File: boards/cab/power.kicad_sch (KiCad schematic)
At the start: 15 parts, among them U1 XL1509-5.0, U2 XL1509-ADJ

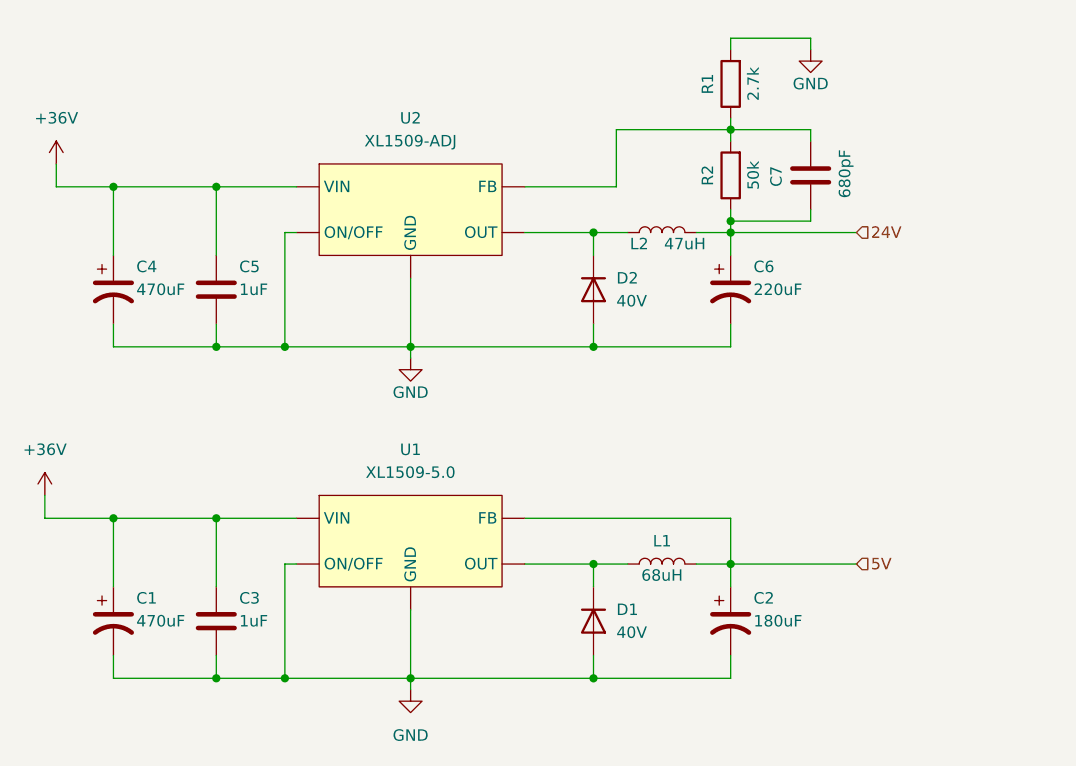
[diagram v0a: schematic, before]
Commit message: Removed hierarchy and added Connectors, Leds
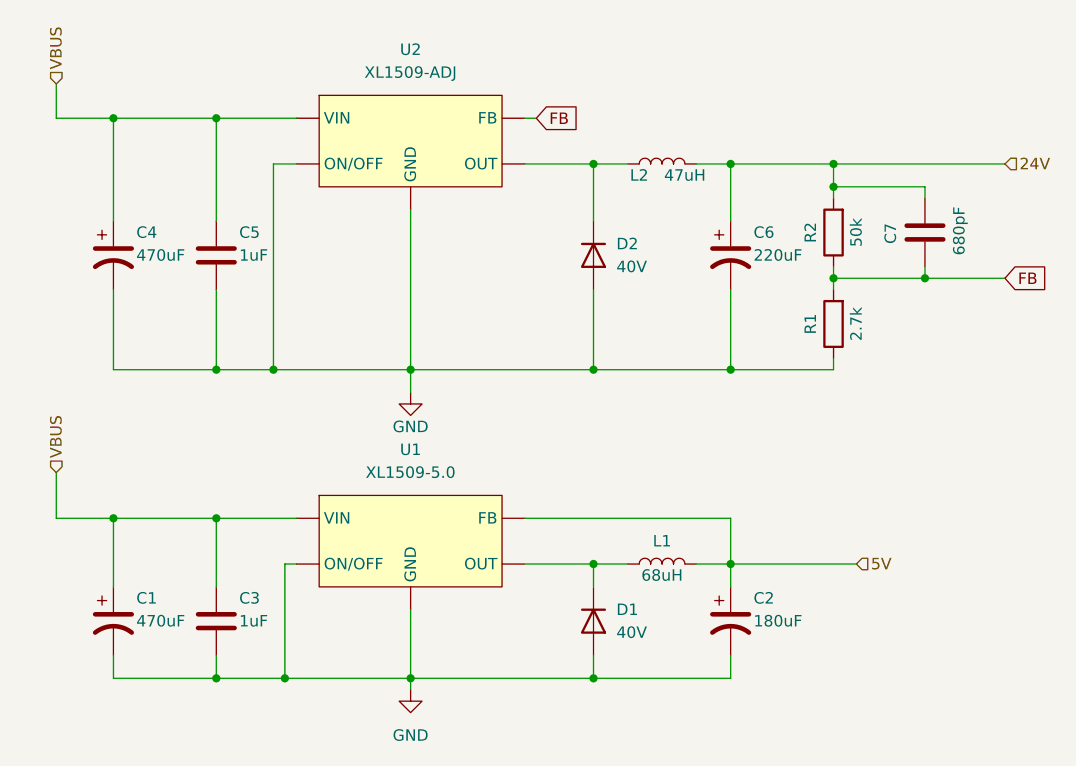
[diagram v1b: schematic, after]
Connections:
- net 24V: now also C7.1, R2.2; no longer C7.2, R2.1
- net GND: now also R1.1; no longer R1.2
- net +36V renamed VBUS
- new net FB: C7.2, R1.2, R2.1, U2. (VIN)
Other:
- moved on the sheet: C4, C5, C6, C7, D2, L2, R1, R2, U2
